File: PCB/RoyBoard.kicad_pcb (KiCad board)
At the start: 2 copper layers, 369.5 x 136.6 mm, 181 parts, among them SW1 SW_Push, SW10 SW_Push, SW11 SW_Push, SW12 SW_Push, SW13 SW_Push, SW14 SW_Push, SW15 SW_Push, SW16 SW_Push, SW17 SW_Push, SW18 SW_Push, SW19 SW_Push, SW2 SW_Push, SW20 SW_Push, SW21 SW_Push, SW22 SW_Push, SW23 SW_Push, SW24 SW_Push, SW25 SW_Push, SW26 SW_Push, SW27 SW_Push, SW28 SW_Push, SW29 SW_Push, SW3 SW_Push, SW30 SW_Push, SW31 SW_Push, SW32 SW_Push, SW33 SW_Push, SW34 SW_Push, SW35 SW_Push, SW36 SW_Push, SW37 SW_Push, SW38 SW_Push, SW39 SW_Push, SW4 SW_Push, SW40 SW_Push, SW41 SW_Push, SW42 SW_Push, SW43 SW_Push, SW44 SW_Push, SW45 SW_Push, SW46 SW_Push, SW47 SW_Push, SW48 SW_Push, SW49 SW_Push, SW5 SW_Push, SW50 SW_Push, SW51 SW_Push, SW52 SW_Push, SW53 SW_Push, SW54 SW_Push, SW55 SW_Push, SW56 SW_Push, SW57 SW_Push, SW58 SW_Push, SW59 SW_Push, SW6 SW_Push, SW60 SW_Push, SW61 SW_Push, SW62 SW_Push, SW63 SW_Push, SW64 SW_Push, SW65 SW_Push, SW66 SW_Push, SW67 SW_Push, SW68 SW_Push, SW69 SW_Push, SW7 SW_Push, SW70 SW_Push, SW71 SW_Push, SW72 SW_Push, SW73 SW_Push, SW74 SW_Push, SW75 SW_Push, SW76 SW_Push, SW77 SW_Push, SW78 SW_Push, SW79 SW_Push, SW8 SW_Push, SW80 SW_Push, SW81 SW_Push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

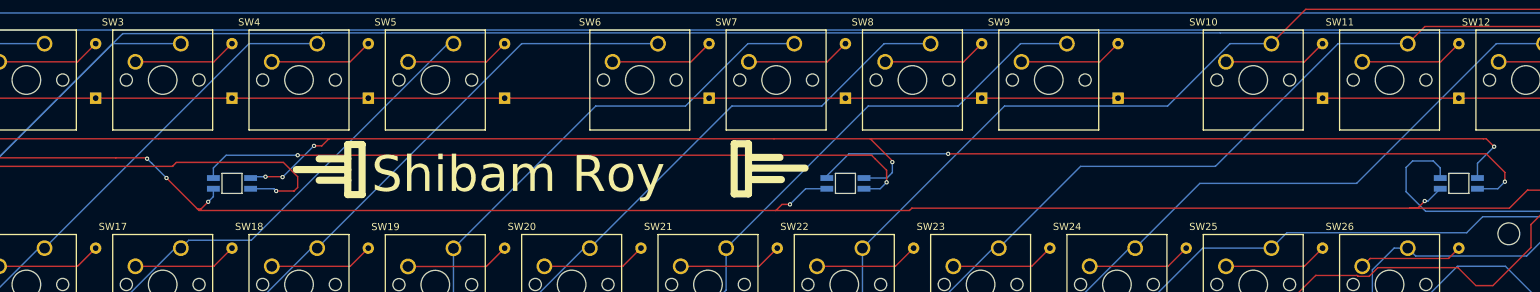
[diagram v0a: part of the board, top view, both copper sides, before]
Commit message: track step files with Git LFS
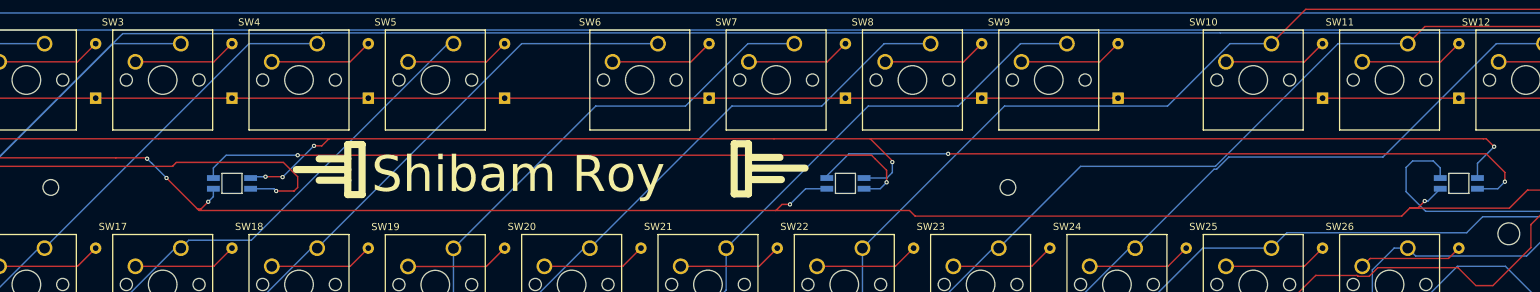
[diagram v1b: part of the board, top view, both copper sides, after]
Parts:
- added REF**: MountingHole_2.2mm_M2, MountingHole:MountingHole_2.2mm_M2, F.Cu at (223.1, 60.4)
- added REF**: MountingHole_2.2mm_M2, MountingHole:MountingHole_2.2mm_M2, F.Cu at (89.4, 60.4)
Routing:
- net GND: track 947.7 -> 948.4 mm
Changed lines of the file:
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@@
 		)
 	)
+	(footprint "MountingHole:MountingHole_2.2mm_M2"
+		(layer "F.Cu")
+		(at 223.135 60.42)
+		(descr "Mounting Hole 2.2mm, M2, no annular, generated by kicad-footprint-generator mountinghole.py")
+		(tags "mountinghole M2")
+		(property "Reference" "REF**"
+			(at 0 -3.15 0)
+			(layer "F.SilkS")
+			(hide yes)
+			(effects
+				(font
+					(size 1 1)
+					(thickness 0.15)
+				)
+			)
+		)
+		(property "Value" "MountingHole_2.2mm_M2"
+			(at 0 3.15 0)
+			(layer "F.Fab")
+			(effects
+				(font
+					(size 1 1)
+					(thickness 0.15)
+				)
+			)
+		)
+		(property "Datasheet" ""
+			(at 0 0 0)
+			(layer "F.Fab")
+			(hide yes)
+			(effects
+				(font
+					(size 1.27 1.27)
+					(thickness 0.15)
+				)
+			)
+		)
+		(property "Description" ""
+			(at 0 0 0)
+			(layer "F.Fab")
+			(hide yes)
+			(effects
+				(font
+					(size 1.27 1.27)
+					(thickness 0.15)
+				)
+			)
+		)
+		(attr exclude_from_pos_files exclude_from_bom)
+		(fp_circle
+			(center 0 0)
+			(end 2.2 0)
+			(stroke
+				(width 0.15)
+				(type solid)
+			)
+			(fill no)
+			(layer "Cmts.User")
+		)
+		(fp_circle
+			(center 0 0)
+			(end 2.45 0)
+			(stroke
+				(width 0.05)
+				(type solid)
+			)
+			(fill no)
+			(layer "F.CrtYd")
+		)
+		(pad "" np_thru_hole circle
+			(at 0 0)
+			(size 2.2 2.2)
+			(drill 2.2)
+			(layers "*.Cu" "*.Mask")
+		)
+		(embedded_fonts no)
+	)
 	(footprint "royboard_footprints:SW_Cherry_MX_1.00u_PCB"
 		(layer "F.Cu")
@@
 		)
 	)
+	(footprint "MountingHole:MountingHole_2.2mm_M2"
+		(layer "F.Cu")
+		(at 89.385 60.42)
+		(descr "Mounting Hole 2.2mm, M2, no annular, generated by kicad-footprint-generator mountinghole.py")
+		(tags "mountinghole M2")
+		(property "Reference" "REF**"
+			(at 0 -3.15 0)
+			(layer "F.SilkS")
+			(hide yes)
+			(effects
+				(font
+					(size 1 1)
+					(thickness 0.15)
+				)
+			)
+		)
+		(property "Value" "MountingHole_2.2mm_M2"
+			(at 0 3.15 0)
+			(layer "F.Fab")
+			(effects
+				(font
+					(size 1 1)
+					(thickness 0.15)
+				)
+			)
+		)
+		(property "Datasheet" ""
+			(at 0 0 0)
+			(layer "F.Fab")
+			(hide yes)
+			(effects
+				(font
+					(size 1.27 1.27)
+					(thickness 0.15)
+				)
+			)
+		)
+		(property "Description" ""
+			(at 0 0 0)
+			(layer "F.Fab")
+			(hide yes)
+			(effects
+				(font
+					(size 1.27 1.27)
+					(thickness 0.15)
+				)
+			)
+		)
+		(attr exclude_from_pos_files exclude_from_bom)
+		(fp_circle
+			(center 0 0)
+			(end 2.2 0)
+			(stroke
+				(width 0.15)
+				(type solid)
+			)
+			(fill no)
+			(layer "Cmts.User")
+		)
+		(fp_circle
+			(center 0 0)
+			(end 2.45 0)
+			(stroke
+				(width 0.05)
+				(type solid)
+			)
+			(fill no)
+			(layer "F.CrtYd")
+		)
+		(pad "" np_thru_hole circle
+			(at 0 0)
+			(size 2.2 2.2)
+			(drill 2.2)
+			(layers "*.Cu" "*.Mask")
+		)
+		(embedded_fonts no)
+	)
 	(footprint "royboard_footprints:SW_Cherry_MX_1.00u_PCB"
 		(layer "F.Cu")
@@
 	)
 	(segment
+		(start 190.715 63.64)
+		(end 209.385 63.64)
+		(width 0.2)
+		(layer "F.Cu")
+		(net 91)
+	)
+	(segment
 		(start 397.425 93.67)
 		(end 397.495 93.6)
@@
 	)
 	(segment
-		(start 190.715 63.64)
-		(end 209.385 63.64)
-		(width 0.2)
-		(layer "F.Cu")
-		(net 91)
-	)
-	(segment
 		(start 394.985 155.69)
 		(end 389.18 161.495)
@@
 	)
 	(segment
-		(start 209.715 63.31)
-		(end 279.285 63.31)
+		(start 209.385 63.64)
+		(end 210.165 64.42)
 		(width 0.2)
 		(layer "F.Cu")
@@
 	)
 	(segment
+		(start 278.175 64.42)
+		(end 279.285 63.31)
+		(width 0.2)
+		(layer "F.Cu")
+		(net 91)
+	)
+	(segment
 		(start 369.504515 117.880485)
 		(end 368.81403 117.19)
@@
 	)
 	(segment
+		(start 210.165 64.42)
+		(end 278.175 64.42)
+		(width 0.2)
+		(layer "F.Cu")
+		(net 91)
+	)
+	(segment
 		(start 191.565 62.79)
 		(end 192.675 62.79)
@@
 		(net 91)
 	)
-	(segment
-		(start 209.385 63.64)
-		(end 209.715 63.31)
-		(width 0.2)
-		(layer "F.Cu")
-		(net 91)
-	)
 	(via
 		(at 394.675 82.53)
@@
 	)
 	(segment
-		(start 291.3925 40.325)
-		(end 298.06 40.325)
-		(width 0.2)
-		(layer "B.Cu")
-		(net 110)
-	)
-	(segment
 		(start 200.42875 98.956434)
 		(end 211.420184 87.965)
@@
 	)
 	(segment
+		(start 251.939 57.871)
+		(end 252.29957 57.871)
+		(width 0.2)
+		(layer "B.Cu")
+		(net 110)
+	)
+	(segment
 		(start 260.7575 147.62)
 		(end 260.7575 151.13625)
@@
 	)
 	(segment
+		(start 291.3925 40.325)
+		(end 298.06 40.325)
+		(width 0.2)
+		(layer "B.Cu")
+		(net 110)
+	)
+	(segment
 		(start 355.21 50.32625)
 		(end 364.735 50.32625)
@@
 	)
 	(segment
-		(start 271.86625 59.85125)
+		(start 275.5475 56.17)
 		(end 291.3925 40.325)
 		(width 0.2)
@@
 	)
 	(segment
-		(start 169.4725 126.05)
-		(end 178.9975 116.525)
+		(start 252.29957 57.871)
+		(end 254.00057 56.17)
 		(width 0.2)
 		(layer "B.Cu")
@@
 	)
 	(segment
-		(start 212.205 87.965)
-		(end 216.50625 83.66375)
+		(start 254.00057 56.17)
+		(end 275.5475 56.17)
 		(width 0.2)
 		(layer "B.Cu")
@@
 	)
 	(segment
-		(start 251.536 153.821)
-		(end 248.05375 150.33875)
+		(start 240.91 68.9)
+		(end 251.939 57.871)
 		(width 0.2)
 		(layer "B.Cu")
@@
 	)
 	(segment
-		(start 249.95875 59.85125)
-		(end 271.86625 59.85125)
+		(start 169.4725 126.05)
+		(end 178.9975 116.525)
 		(width 0.2)
 		(layer "B.Cu")
@@
 	)
 	(segment
-		(start 364.735 50.32625)
-		(end 369.4975 55.08875)
+		(start 212.205 87.965)
+		(end 216.50625 83.66375)
 		(width 0.2)
 		(layer "B.Cu")
@@
 	)
 	(segment
-		(start 240.91 68.9)
-		(end 249.95875 59.85125)
+		(start 251.536 153.821)
+		(end 248.05375 150.33875)
+		(width 0.2)
+		(layer "B.Cu")
+		(net 110)
+	)
+	(segment
+		(start 364.735 50.32625)
+		(end 369.4975 55.08875)
 		(width 0.2)
 		(layer "B.Cu")
